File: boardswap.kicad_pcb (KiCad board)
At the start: 2 copper layers, 285 x 96.1 mm, 155 parts, among them J1 USB_C_Receptacle_USB2.0, SW1 SW_Push, U1 ATmega32U4-AU, Y1 16MHz

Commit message: fix
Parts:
- moved SW1 0.45 mm to (8.78, -176.2), turned to 180 degrees
- turned U1 to 45 degrees

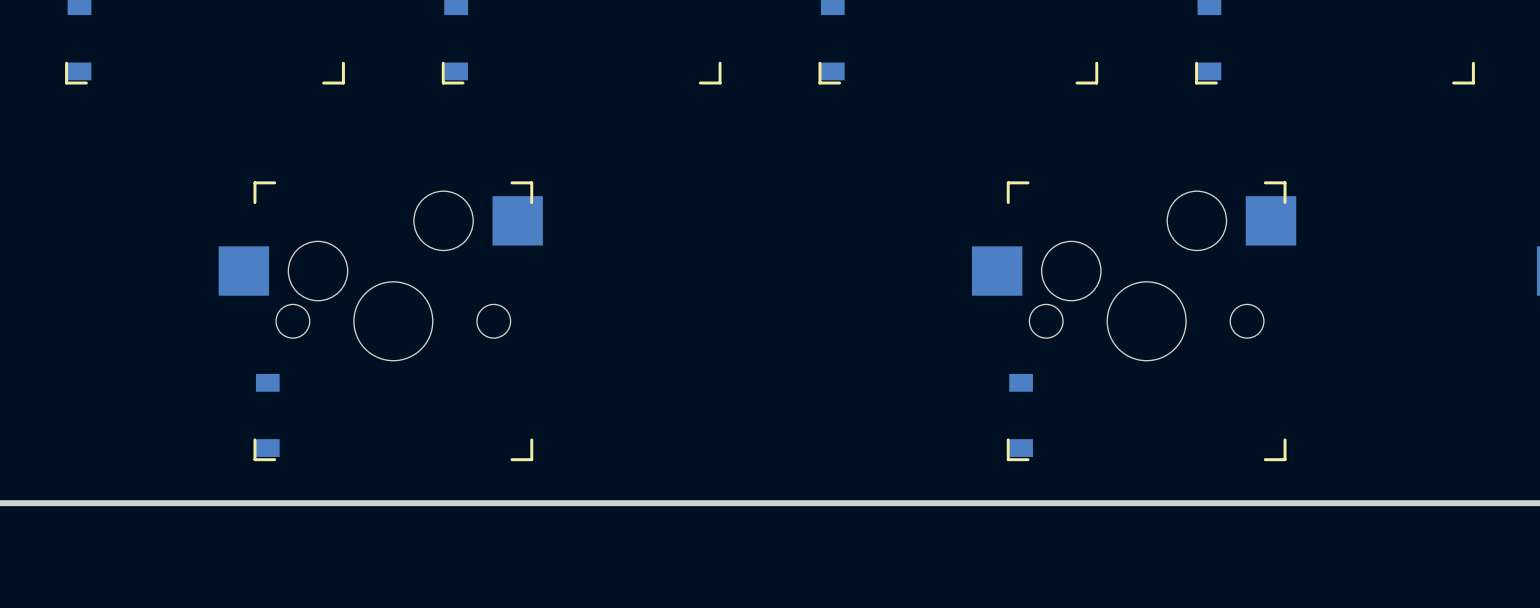
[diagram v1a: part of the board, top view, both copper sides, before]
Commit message: added stabs
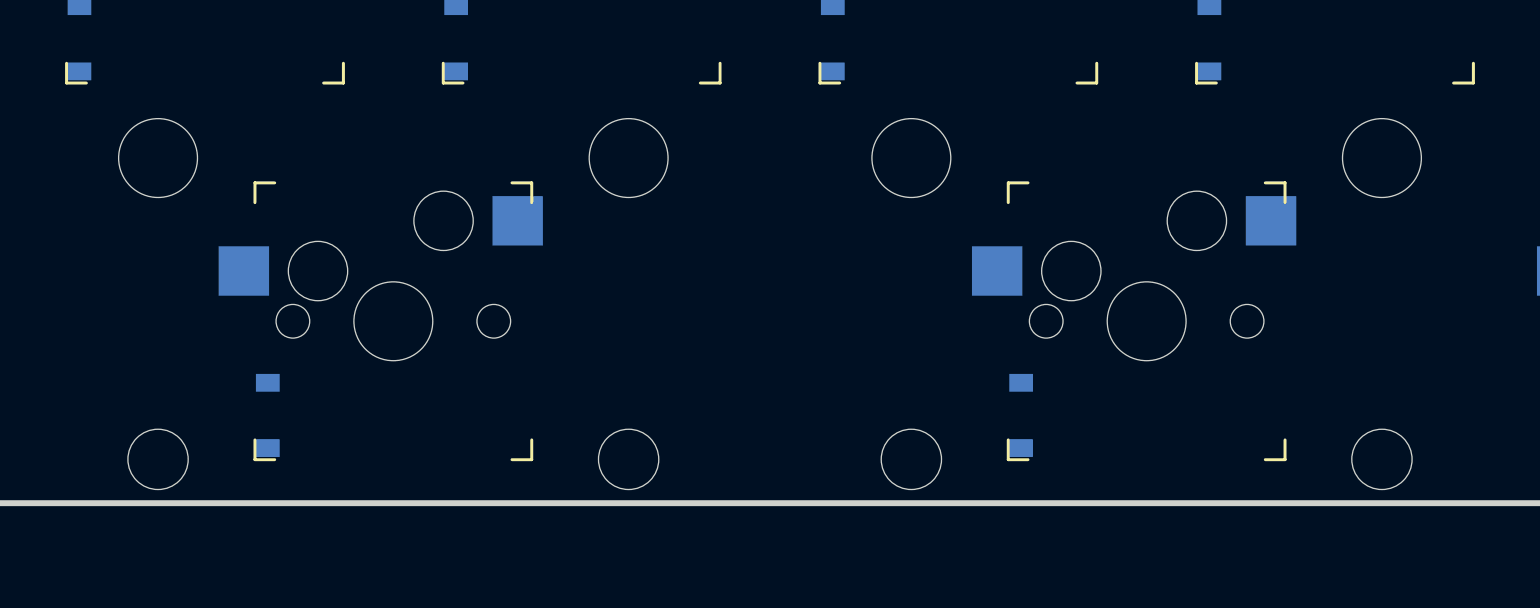
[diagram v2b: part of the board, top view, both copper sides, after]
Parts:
- added REF**: Stabilizer_MX_2u, keyswitches:Stabilizer_MX_2u, F.Cu at (142.9, -138.1)
- added REF**: Stabilizer_MX_2u, keyswitches:Stabilizer_MX_2u, F.Cu at (104.8, -138.1)

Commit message: placed components
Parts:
- C1, C2, C3, R1, R2, R3, R4, R5, R6, Y1: moved to B.Cu
- C4, C5, C6, C7: footprint Capacitor_SMD:C_0805_2012Metric -> Capacitor_SMD:C_0603_1608Metric; moved to B.Cu
- moved R3 142.7 mm to (8.93, -208.4), turned to 90 degrees
- moved C3 119.2 mm to (4.76, -160.5), turned to 90 degrees
- moved R5 113.7 mm to (-12.5, -214.3), turned to 90 degrees
- moved R2 102.8 mm to (5.95, -208.4), turned to 90 degrees
- moved C6 101.3 mm to (7.74, -139.9)
- moved C7 99.3 mm to (16.1, -145.9)
- moved R4 95.2 mm to (10.7, -163.7), turned to 270 degrees
- moved R6 93.5 mm to (-15.5, -214.3), turned to 90 degrees
- moved C5 83.9 mm to (7.55, -161.3), turned to 180 degrees
- moved C2 80.3 mm to (-8.93, -147.6)
- moved C4 70.3 mm to (7.55, -159.5), turned to 180 degrees
- moved R1 48.9 mm to (-1.19, -146.4), turned to 180 degrees
- moved Y1 46.5 mm to (-4.67, -149.2), turned to 180 degrees
- moved C1 42.9 mm to (-8.93, -150.0), turned to 180 degrees
- moved SW1 41.7 mm to (7.02, -134.5), turned to 0 degrees
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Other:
- net class Power: trace_width 0.381 -> 0.254

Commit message: routed everything except matrix to mcu
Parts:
- moved D30 9.56 mm to (18.2, -171.4), turned to 180 degrees
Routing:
- net ROW3: track 0.00 -> 291.5 mm, vias 0 -> 6
- net ROW0: track 0.00 -> 284.7 mm, vias 0 -> 4
- net ROW2: track 0.00 -> 267.2 mm, vias 0 -> 2
- net ROW1: track 0.00 -> 267.0 mm
- net ROW4: track 0.00 -> 266.1 mm
- net GND: track 0.00 -> 125.2 mm, vias 0 -> 5
- net +5V: track 0.00 -> 116.5 mm, vias 0 -> 8
- net COL13: track 0.00 -> 90.8 mm, vias 0 -> 2
- net COL7: track 0.00 -> 80.4 mm, vias 0 -> 8
- net COL5: track 0.00 -> 80.3 mm, vias 0 -> 8
- net COL0: track 0.00 -> 77.9 mm, vias 0 -> 4
- net COL12: track 0.00 -> 77.6 mm, vias 0 -> 8
- net COL1: track 0.00 -> 76.7 mm, vias 0 -> 8
- net COL2: track 0.00 -> 76.6 mm, vias 0 -> 8
- net COL10: track 0.00 -> 76.5 mm, vias 0 -> 8
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- added copper zone on B.Cu, net GND
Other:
- net class Power: trace_width 0.254 -> 0.381

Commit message: done routing probably
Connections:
- U1 pad 1: Net-(U1-Pad1) -> COL5
- U1 pad 10: Net-(U1-Pad10) -> COL2
- U1 pad 11: Net-(U1-Pad11) -> COL0
- U1 pad 18: Net-(U1-Pad18) -> ROW4
- U1 pad 19: Net-(U1-Pad19) -> ROW0
- U1 pad 20: Net-(U1-Pad20) -> ROW1
- U1 pad 21: Net-(U1-Pad21) -> ROW2
- U1 pad 22: Net-(U1-Pad22) -> ROW3
- U1 pad 28: Net-(U1-Pad28) -> COL13
- U1 pad 30: Net-(U1-Pad30) -> COL12
- U1 pad 36: Net-(U1-Pad36) -> COL11
- U1 pad 37: Net-(U1-Pad37) -> COL10
- U1 pad 38: Net-(U1-Pad38) -> COL9
- U1 pad 39: Net-(U1-Pad39) -> COL8
- U1 pad 40: Net-(U1-Pad40) -> COL7
- U1 pad 41: Net-(U1-Pad41) -> COL6
- U1 pad 8: Net-(U1-Pad8) -> COL4
- U1 pad 9: Net-(U1-Pad9) -> COL3
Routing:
- net COL13: track 90.8 -> 355.5 mm, vias 2 -> 4
- net COL12: track 77.6 -> 317.2 mm, vias 8 -> 10
- net COL11: track 76.5 -> 289.3 mm, vias 8 -> 10
- net COL10: track 76.5 -> 270.3 mm, vias 8 -> 10
- net COL9: track 76.4 -> 254.1 mm, vias 8 -> 10
- net COL8: track 57.3 -> 215.6 mm, vias 6 -> 8
- net COL7: track 80.4 -> 219.1 mm, vias 8 -> 10
- net COL6: track 57.3 -> 178.0 mm, vias 6 -> 10
- net COL5: track 80.3 -> 186.0 mm, vias 8 -> 12
- net ROW0: track 284.7 -> 381.9 mm, vias 4 -> 8
- net COL4: track 76.5 -> 166.5 mm, vias 8 -> 12
- net COL3: track 76.5 -> 150.0 mm, vias 8 -> 12
- net ROW1: track 267.0 -> 335.3 mm, vias 0 -> 4
- net COL2: track 76.6 -> 131.8 mm, vias 8 -> 10
- net ROW2: track 267.2 -> 311.9 mm, vias 2 -> 6
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
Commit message: added fill
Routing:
- added copper zone on B.Cu, net (none)
- added copper zone on F.Cu, net (none)

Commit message: rotated mcu, begrudgingly
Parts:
- moved C2 31.1 mm to (22.2, -148.8), turned to 270 degrees
- moved C1 27.6 mm to (18.4, -146.3), turned to 0 degrees
- moved Y1 23.6 mm to (18.9, -149.0), turned to 0 degrees
- moved R4 23.0 mm to (4.28, -141.7), turned to 90 degrees
- moved C7 16.7 mm to (-0.59, -146.9), turned to 90 degrees
- moved C6 12.2 mm to (-2.22, -146.9), turned to 90 degrees
- moved R1 10.7 mm to (7.54, -140.3), turned to 0 degrees
- moved R3 4.03 mm to (4.90, -208.5)
- moved R2 1.15 mm to (7.10, -208.5)
- moved SW1 1.09 mm to (7.21, -135.6)
- moved C4 0.23 mm to (7.49, -159.8)
- moved C3 0.13 mm to (4.88, -160.5)
- moved C5 0.08 mm to (7.48, -161.4)
- turned U1 to 270 degrees
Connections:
- U1 pad 1: COL5 -> COL0
- U1 pad 10: COL2 -> COL11
- U1 pad 11: COL0 -> COL10
- U1 pad 12: Net-(U1-Pad12) -> COL9
- U1 pad 18: ROW4 -> COL6
- U1 pad 19: ROW0 -> COL5
- U1 pad 20: ROW1 -> COL4
- U1 pad 21: ROW2 -> COL3
- U1 pad 22: ROW3 -> COL2
- U1 pad 25: Net-(U1-Pad25) -> COL8
- U1 pad 26: Net-(U1-Pad26) -> COL7
- U1 pad 28: COL13 -> Net-(U1-Pad28)
- U1 pad 30: COL12 -> Net-(U1-Pad30)
- U1 pad 36: COL11 -> Net-(U1-Pad36)
- U1 pad 37: COL10 -> ROW4
- U1 pad 38: COL9 -> ROW0
- U1 pad 39: COL8 -> ROW1
- U1 pad 40: COL7 -> ROW2
- U1 pad 41: COL6 -> ROW3
- U1 pad 8: COL4 -> COL13
- U1 pad 9: COL3 -> COL12
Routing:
- net Net-(R1-Pad1): track 20.6 -> 56.4 mm, vias 2 -> 6
- net COL2: track 131.8 -> 109.1 mm
- net COL3: track 150.0 -> 128.3 mm
- net GND: track 125.2 -> 146.8 mm, vias 5 -> 9
- net COL4: track 166.5 -> 147.5 mm
- net Net-(R2-Pad1): track 74.5 -> 56.4 mm
- net Net-(R3-Pad1): track 72.4 -> 55.2 mm
- net Net-(C3-Pad1): track 22.2 -> 5.52 mm, vias 2 -> 0
- net COL7: track 219.1 -> 233.9 mm
- net D-: track 27.3 -> 14.1 mm
- net COL8: track 215.6 -> 228.5 mm
- net ROW2: track 311.9 -> 303.5 mm, vias 6 -> 4
- net D+: track 23.1 -> 15.7 mm, vias 2 -> 0
- net COL9: track 254.1 -> 247.4 mm
- net Net-(R4-Pad2): track 8.91 -> 2.29 mm
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- removed copper zone on B.Cu, net (none)
- removed copper zone on F.Cu, net (none)

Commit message: fixed silkscreen
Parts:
- MX1, MX10, MX11, MX12, MX13, MX14, MX15, MX16, MX17, MX18, MX19, MX2, MX20, MX21, MX22, MX23, MX24, MX25, MX26, MX27, MX28, MX29, MX3, MX30, MX31, MX32, MX33, MX34, MX35, MX36, MX37, MX38, MX39, MX4, MX40, MX41, MX42, MX43, MX44, MX45, MX46, MX47, MX48, MX49, MX5, MX50, MX51, MX52, MX53, MX54, MX55, MX56, MX57, MX58, MX59, MX6, MX60, MX61, MX62, MX63, MX64, MX65, MX66, MX67, MX68, MX7, MX8, MX9: footprint keyswitches:Kailh_socket_MX -> keyswitches:Kailh_socket_MX_alt
- R5, R6: value 10K -> 5.1K
